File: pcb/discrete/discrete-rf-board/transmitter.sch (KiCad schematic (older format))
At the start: 7 parts

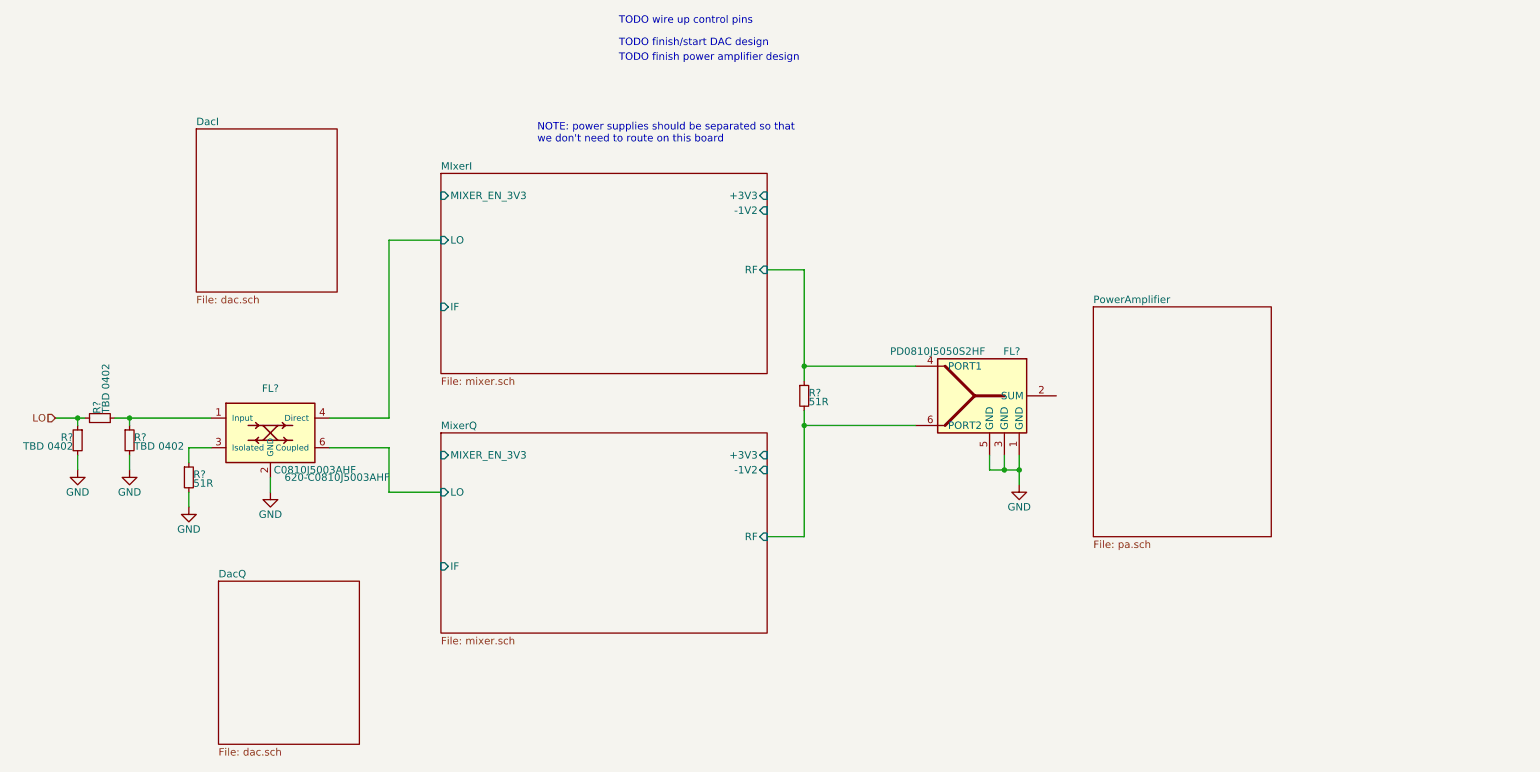
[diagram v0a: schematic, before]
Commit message: Design DAC/ADC stages, pass out all control signals to top sheet
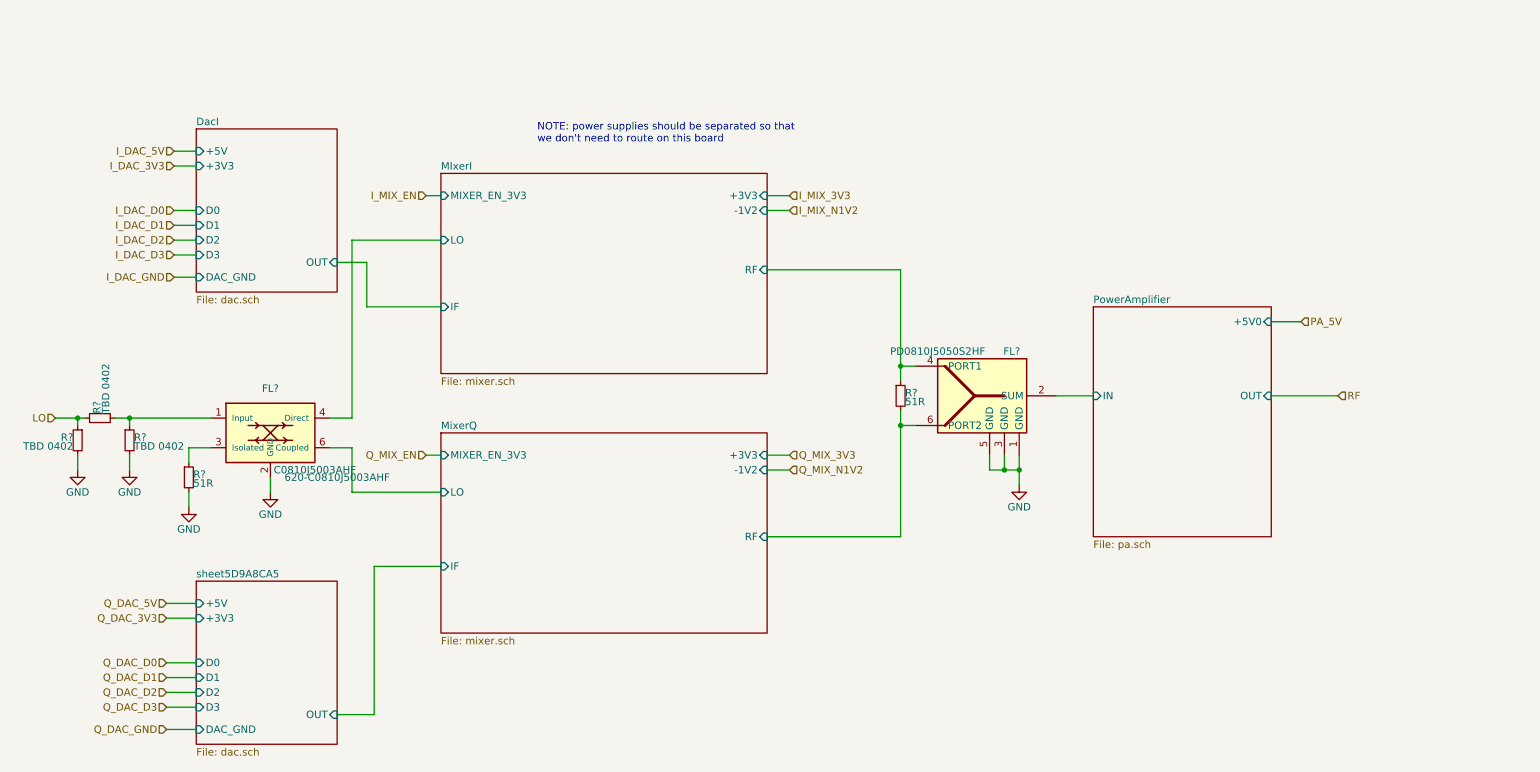
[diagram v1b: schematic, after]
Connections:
- net PowerAmplifier/IN: now reaches FL?.2 (SUM)
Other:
- note removed: "TODO finish power amplifier design"
- note removed: "TODO finish/start DAC design"
- note removed: "TODO wire up control pins"
- moved on the sheet: R?
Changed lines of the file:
@@
 $Descr A4 11693 8268
 encoding utf-8
-Sheet 13 19
+Sheet 2 19
 Title ""
 Date ""
@@
 $EndComp
 Wire Wire Line
-	6850 3350 6100 3350
-Wire Wire Line
-	6100 3350 6100 2700
-Wire Wire Line
-	6100 2700 5850 2700
-Wire Wire Line
-	5850 4500 6100 4500
-Wire Wire Line
-	6100 4500 6100 3750
-Wire Wire Line
-	6100 3750 6850 3750
+	6850 3350 6750 3350
+Wire Wire Line
+	6750 3350 6750 2700
+Wire Wire Line
+	6750 2700 5850 2700
+Wire Wire Line
+	5850 4500 6750 4500
+Wire Wire Line
+	6750 4500 6750 3750
+Wire Wire Line
+	6750 3750 6850 3750
 $Comp
 L Device:R_Small R?
 U 1 1 5D7F54C0
-P 6100 3550
-F 0 "R?" H 6130 3570 50  0000 L CNN
-F 1 "51R" H 6130 3510 50  0000 L CNN
-F 2 "" H 6100 3550 50  0001 C CNN
-F 3 "~" H 6100 3550 50  0001 C CNN
-	1    6100 3550
-	1    0    0    -1
-$EndComp
-Wire Wire Line
-	6100 3650 6100 3750
-Connection ~ 6100 3750
-Wire Wire Line
-	6100 3450 6100 3350
-Connection ~ 6100 3350
+P 6750 3550
+F 0 "R?" H 6780 3570 50  0000 L CNN
+F 1 "51R" H 6780 3510 50  0000 L CNN
+F 2 "" H 6750 3550 50  0001 C CNN
+F 3 "~" H 6750 3550 50  0001 C CNN
+	1    6750 3550
+	1    0    0    -1
+$EndComp
+Wire Wire Line
+	6750 3650 6750 3750
+Connection ~ 6750 3750
+Wire Wire Line
+	6750 3450 6750 3350
+Connection ~ 6750 3350
 $Comp
 L power:GND #PWR?
@@
 Connection ~ 7450 4050
 Wire Wire Line
-	3300 4200 3650 4200
-Wire Wire Line
-	3300 3900 3300 4200
-Wire Wire Line
-	3300 2500 3650 2500
+	3050 4200 3650 4200
+Wire Wire Line
+	3050 3900 3050 4200
+Wire Wire Line
+	3050 2500 3650 2500
 Text HLabel 1050 3700 0    50   Input ~ 0
 LO
@@
 F0 "PowerAmplifier" 50
 F1 "pa.sch" 50
+F2 "IN" I L 8050 3550 50
+F3 "OUT" I R 9250 3550 50
+F4 "+5V0" I R 9250 3050 50
 $EndSheet
 $Sheet
@@
 F0 "DacI" 50
 F1 "dac.sch" 50
-$EndSheet
-$Sheet
-S 2150 4800 950  1100
-U 5D8337F2
-F0 "DacQ" 50
-F1 "dac.sch" 50
+F2 "OUT" I R 2950 2650 50
+F3 "+5V" I L 2000 1900 50
+F4 "+3V3" I L 2000 2000 50
+F5 "D0" I L 2000 2300 50
+F6 "D1" I L 2000 2400 50
+F7 "D2" I L 2000 2500 50
+F8 "D3" I L 2000 2600 50
+F9 "DAC_GND" I L 2000 2750 50
 $EndSheet
 $Comp
@@
 	1450 3700 1550 3700
 Wire Wire Line
-	2900 3700 3300 3700
-Wire Wire Line
-	3300 2500 3300 3700
-Wire Wire Line
-	2900 3900 3300 3900
+	2900 3700 3050 3700
+Wire Wire Line
+	3050 2500 3050 3700
+Wire Wire Line
+	2900 3900 3050 3900
 $Comp
 L Device:R_Small R?
@@
 Wire Wire Line
 	2500 4200 2500 4100
-Text Notes 4850 1050 0    50   ~ 0
-TODO wire up control pins
-Text Notes 4850 1200 0    50   ~ 0
-TODO finish/start DAC design
-Text Notes 4850 1300 0    50   ~ 0
-TODO finish power amplifier design
+Wire Wire Line
+	8050 3550 7800 3550
+Text HLabel 9700 3550 2    50   Input ~ 0
+RF
+Wire Wire Line
+	9700 3550 9250 3550
+Wire Wire Line
+	2950 2650 3150 2650
+Wire Wire Line
+	3150 2650 3150 2950
+Wire Wire Line
+	3150 2950 3650 2950
+$Sheet
+S 2000 4800 950  1100
+U 5D9A8CAE
+F0 "sheet5D9A8CA5" 50
+F1 "dac.sch" 50
+F2 "OUT" I R 2950 5700 50
+F3 "+5V" I L 2000 4950 50
+F4 "+3V3" I L 2000 5050 50
+F5 "D0" I L 2000 5350 50
+F6 "D1" I L 2000 5450 50
+F7 "D2" I L 2000 5550 50
+F8 "D3" I L 2000 5650 50
+F9 "DAC_GND" I L 2000 5800 50
+$EndSheet
+Wire Wire Line
+	3200 5700 3200 4700
+Wire Wire Line
+	3200 4700 3650 4700
+Wire Wire Line
+	2950 5700 3200 5700
+Text HLabel 1850 2300 0    50   Input ~ 0
+I_DAC_D0
+Text HLabel 1850 2400 0    50   Input ~ 0
+I_DAC_D1
+Text HLabel 1850 2500 0    50   Input ~ 0
+I_DAC_D2
+Text HLabel 1850 2600 0    50   Input ~ 0
+I_DAC_D3
+Wire Wire Line
+	1850 2300 2000 2300
+Wire Wire Line
+	2000 2400 1850 2400
+Wire Wire Line
+	1850 2500 2000 2500
+Wire Wire Line
+	1850 2600 2000 2600
+Text HLabel 1850 2000 0    50   Input ~ 0
+I_DAC_3V3
+Text HLabel 1850 1900 0    50   Input ~ 0
+I_DAC_5V
+Wire Wire Line
+	1850 1900 2000 1900
+Wire Wire Line
+	2000 2000 1850 2000
+Text HLabel 3550 2200 0    50   Input ~ 0
+I_MIX_EN
+Wire Wire Line
+	3550 2200 3650 2200
+Text HLabel 6000 2200 2    50   Input ~ 0
+I_MIX_3V3
+Text HLabel 6000 2300 2    50   Input ~ 0
+I_MIX_N1V2
+Wire Wire Line
+	6000 2300 5850 2300
+Wire Wire Line
+	5850 2200 6000 2200
+Text HLabel 6000 3950 2    50   Input ~ 0
+Q_MIX_3V3
+Text HLabel 6000 4050 2    50   Input ~ 0
+Q_MIX_N1V2
+Wire Wire Line
+	6000 4050 5850 4050
+Wire Wire Line
+	5850 3950 6000 3950
+Text HLabel 3550 3950 0    50   Input ~ 0
+Q_MIX_EN
+Wire Wire Line
+	3550 3950 3650 3950
+Text HLabel 9450 3050 2    50   Input ~ 0
+PA_5V
+Wire Wire Line
+	9450 3050 9250 3050
+Text HLabel 1800 4950 0    50   Input ~ 0
+Q_DAC_5V
+Text HLabel 1800 5050 0    50   Input ~ 0
+Q_DAC_3V3
+Text HLabel 1800 5350 0    50   Input ~ 0
+Q_DAC_D0
+Text HLabel 1800 5450 0    50   Input ~ 0
+Q_DAC_D1
+Text HLabel 1800 5550 0    50   Input ~ 0
+Q_DAC_D2
+Text HLabel 1800 5650 0    50   Input ~ 0
+Q_DAC_D3
+Wire Wire Line
+	1800 4950 2000 4950
+Wire Wire Line
+	1800 5050 2000 5050
+Wire Wire Line
+	1800 5350 2000 5350
+Wire Wire Line
+	1800 5450 2000 5450
+Wire Wire Line
+	2000 5550 1800 5550
+Wire Wire Line
+	1800 5650 2000 5650
+Text HLabel 1850 2750 0    50   Input ~ 0
+I_DAC_GND
+Wire Wire Line
+	1850 2750 2000 2750
+Text HLabel 1800 5800 0    50   Input ~ 0
+Q_DAC_GND
+Wire Wire Line
+	1800 5800 2000 5800
 $EndSCHEMATC

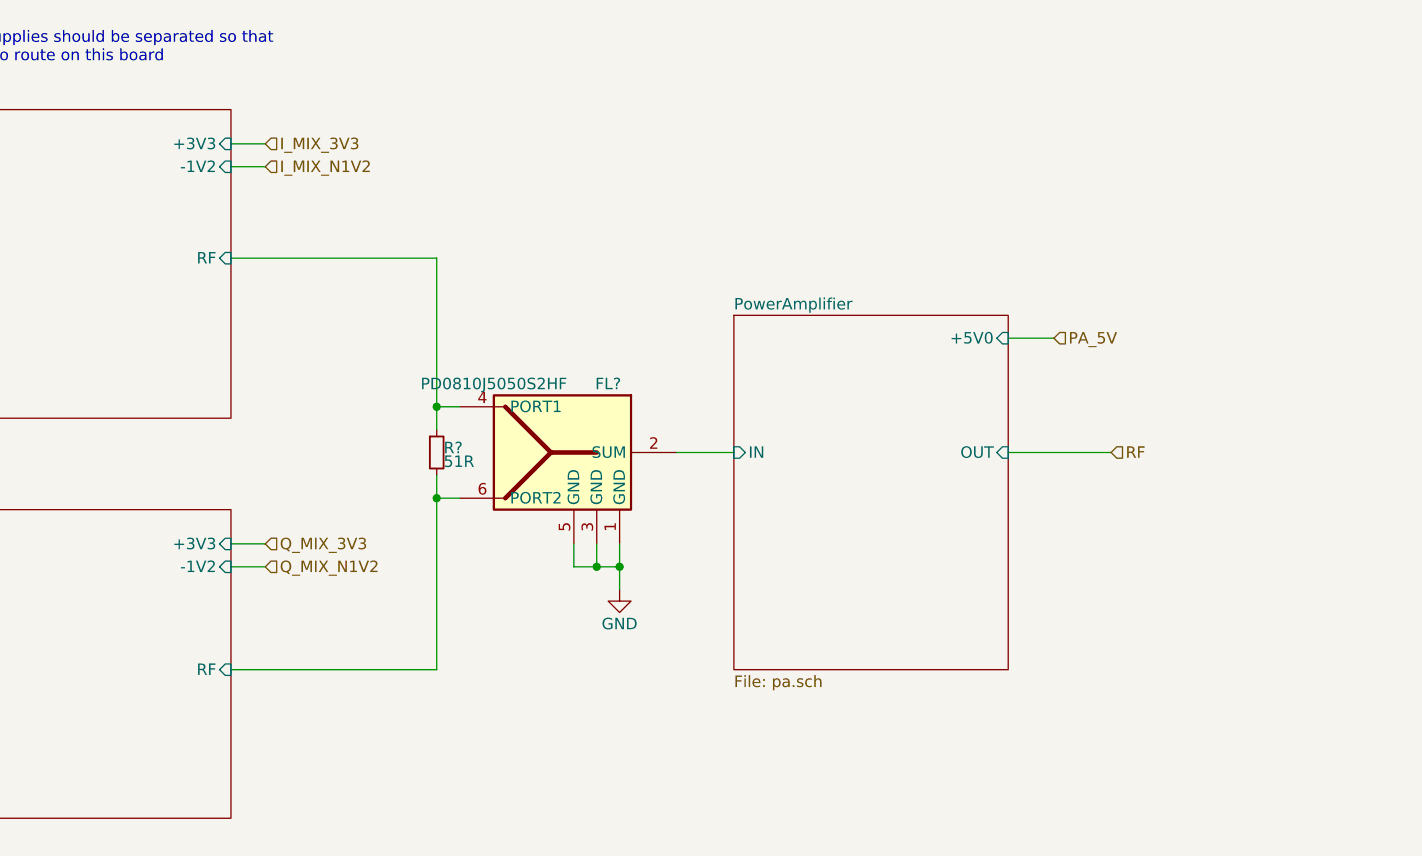
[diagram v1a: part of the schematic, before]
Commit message: Wire out all control signals to connectors TODO PLL charge pump loop, bypass caps in attenuator circuit, antialiasing filter for ADC frontend
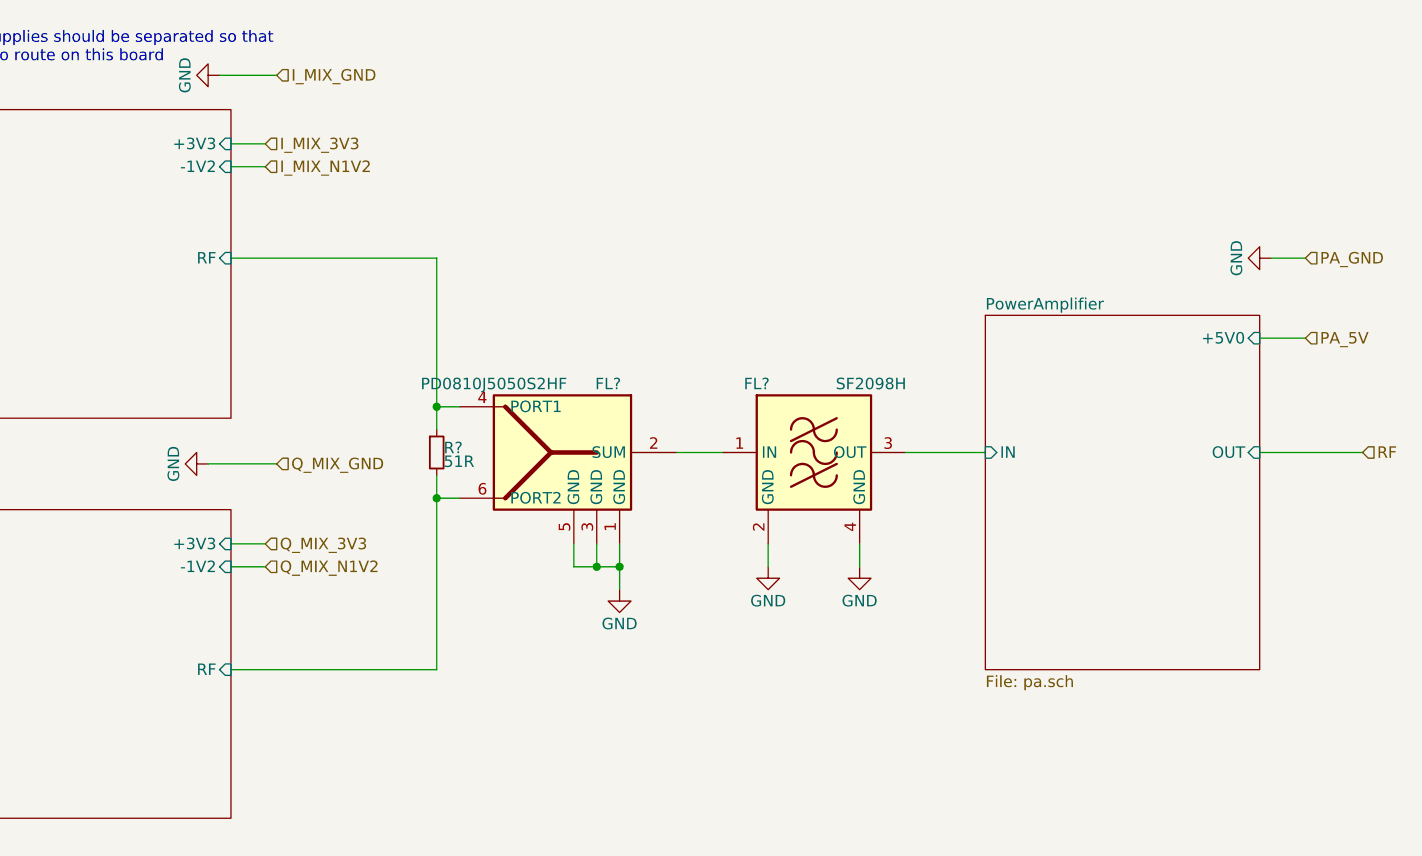
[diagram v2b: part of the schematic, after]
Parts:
- added FL?: SF2098H, symbol discrete-parts:SF2098H
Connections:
- net GND: now also FL?.2 (GND), FL?.4 (GND)
- net PowerAmplifier/IN: now also FL?.3 (OUT); no longer FL?.2 (SUM)
- net at FL?.2 (SUM): now also FL?.1 (IN)
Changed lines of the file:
@@
 	1050 3700 1200 3700
 $Sheet
-S 8050 2950 1200 1550
+S 9150 2950 1200 1550
 U 5D830BD7
 F0 "PowerAmplifier" 50
 F1 "pa.sch" 50
-F2 "IN" I L 8050 3550 50
-F3 "OUT" I R 9250 3550 50
-F4 "+5V0" I R 9250 3050 50
+F2 "IN" I L 9150 3550 50
+F3 "OUT" I R 10350 3550 50
+F4 "+5V0" I R 10350 3050 50
 $EndSheet
 $Sheet
@@
 Wire Wire Line
 	2500 4200 2500 4100
-Wire Wire Line
-	8050 3550 7800 3550
-Text HLabel 9700 3550 2    50   Input ~ 0
+Text HLabel 10800 3550 2    50   Input ~ 0
 RF
 Wire Wire Line
-	9700 3550 9250 3550
+	10800 3550 10350 3550
 Wire Wire Line
 	2950 2650 3150 2650
@@
 Wire Wire Line
 	3550 3950 3650 3950
-Text HLabel 9450 3050 2    50   Input ~ 0
+Text HLabel 10550 3050 2    50   Input ~ 0
 PA_5V
 Wire Wire Line
-	9450 3050 9250 3050
+	10550 3050 10350 3050
 Text HLabel 1800 4950 0    50   Input ~ 0
 Q_DAC_5V
@@
 Wire Wire Line
 	1800 5800 2000 5800
+$Comp
+L discrete-parts:SF2098H FL?
+U 1 1 5DCA527D
+P 8400 3550
+AR Path="/5CA6B0AA/5DCA527D" Ref="FL?"  Part="1"
+AR Path="/5CA6B0B3/5DCA527D" Ref="FL?"  Part="1"
+F 0 "FL?" H 8150 3850 50  0000 C CNN
+F 1 "SF2098H" H 8650 3850 50  0000 C CNN
+F 2 "" H 8400 3100 50  0001 C CNN
+F 3 "" H 8400 3950 50  0001 C CNN
+	1    8400 3550
+	1    0    0    -1
+$EndComp
+Wire Wire Line
+	8800 3550 9150 3550
+Wire Wire Line
+	7800 3550 8000 3550
+$Comp
+L power:GND #PWR?
+U 1 1 5DCABC6C
+P 8200 4050
+F 0 "#PWR?" H 8200 3800 50  0001 C CNN
+F 1 "GND" H 8200 3900 50  0000 C CNN
+F 2 "" H 8200 4050 50  0001 C CNN
+F 3 "" H 8200 4050 50  0001 C CNN
+	1    8200 4050
+	1    0    0    -1
+$EndComp
+$Comp
+L power:GND #PWR?
+U 1 1 5DCABEC4
+P 8600 4050
+F 0 "#PWR?" H 8600 3800 50  0001 C CNN
+F 1 "GND" H 8600 3900 50  0000 C CNN
+F 2 "" H 8600 4050 50  0001 C CNN
+F 3 "" H 8600 4050 50  0001 C CNN
+	1    8600 4050
+	1    0    0    -1
+$EndComp
+Wire Wire Line
+	8600 4050 8600 3950
+Wire Wire Line
+	8200 3950 8200 4050
+Text HLabel 10550 2700 2    50   Input ~ 0
+PA_GND
+$Comp
+L power:GND #PWR?
+U 1 1 5D8EC555
+P 10400 2700
+F 0 "#PWR?" H 10400 2450 50  0001 C CNN
+F 1 "GND" H 10400 2550 50  0000 C CNN
+F 2 "" H 10400 2700 50  0001 C CNN
+F 3 "" H 10400 2700 50  0001 C CNN
+	1    10400 2700
+	0    1    1    0
+$EndComp
+Wire Wire Line
+	10400 2700 10550 2700
+Text HLabel 6050 1900 2    50   Input ~ 0
+I_MIX_GND
+$Comp
+L power:GND #PWR?
+U 1 1 5D8EF6D5
+P 5800 1900
+F 0 "#PWR?" H 5800 1650 50  0001 C CNN
+F 1 "GND" H 5800 1750 50  0000 C CNN
+F 2 "" H 5800 1900 50  0001 C CNN
+F 3 "" H 5800 1900 50  0001 C CNN
+	1    5800 1900
+	0    1    1    0
+$EndComp
+Wire Wire Line
+	5800 1900 6050 1900
+Text HLabel 6050 3600 2    50   Input ~ 0
+Q_MIX_GND
+$Comp
+L power:GND #PWR?
+U 1 1 5D8F1675
+P 5750 3600
+F 0 "#PWR?" H 5750 3350 50  0001 C CNN
+F 1 "GND" H 5750 3450 50  0000 C CNN
+F 2 "" H 5750 3600 50  0001 C CNN
+F 3 "" H 5750 3600 50  0001 C CNN
+	1    5750 3600
+	0    1    1    0
+$EndComp
+Wire Wire Line
+	5750 3600 6050 3600
 $EndSCHEMATC

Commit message: The footprintening continues
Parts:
- R?: value 51R -> 51R 0603
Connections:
- net at FL?.2 (SUM): now also FL?.1 (IN)
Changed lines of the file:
@@
 P 6750 3550
 F 0 "R?" H 6780 3570 50  0000 L CNN
-F 1 "51R" H 6780 3510 50  0000 L CNN
+F 1 "51R 0603" H 6780 3510 50  0000 L CNN
 F 2 "" H 6750 3550 50  0001 C CNN
 F 3 "~" H 6750 3550 50  0001 C CNN
